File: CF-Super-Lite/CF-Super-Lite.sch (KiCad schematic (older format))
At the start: 12 parts, among them J1 IDE_CONNECTOR, J2 CF Adapter Power, J3 Bus_ISA_8bit, SW1 DIP Switch x3 or x4, U1 BIOS FLASH, U2 74HCT245, U3 GAL16V8

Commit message: CF-Super-Lite: Final board tweaks before sending to production.
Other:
- note removed: "TODO: Need to handle RESET signal."
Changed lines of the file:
@@
 NoConn ~ 2000 2000
 NoConn ~ 2000 2200
-Text Notes 750  6400 0    118  ~ 0
-TODO: Need to handle RESET signal.
 Text GLabel 4050 2300 0    50   Input ~ 0
 RESET

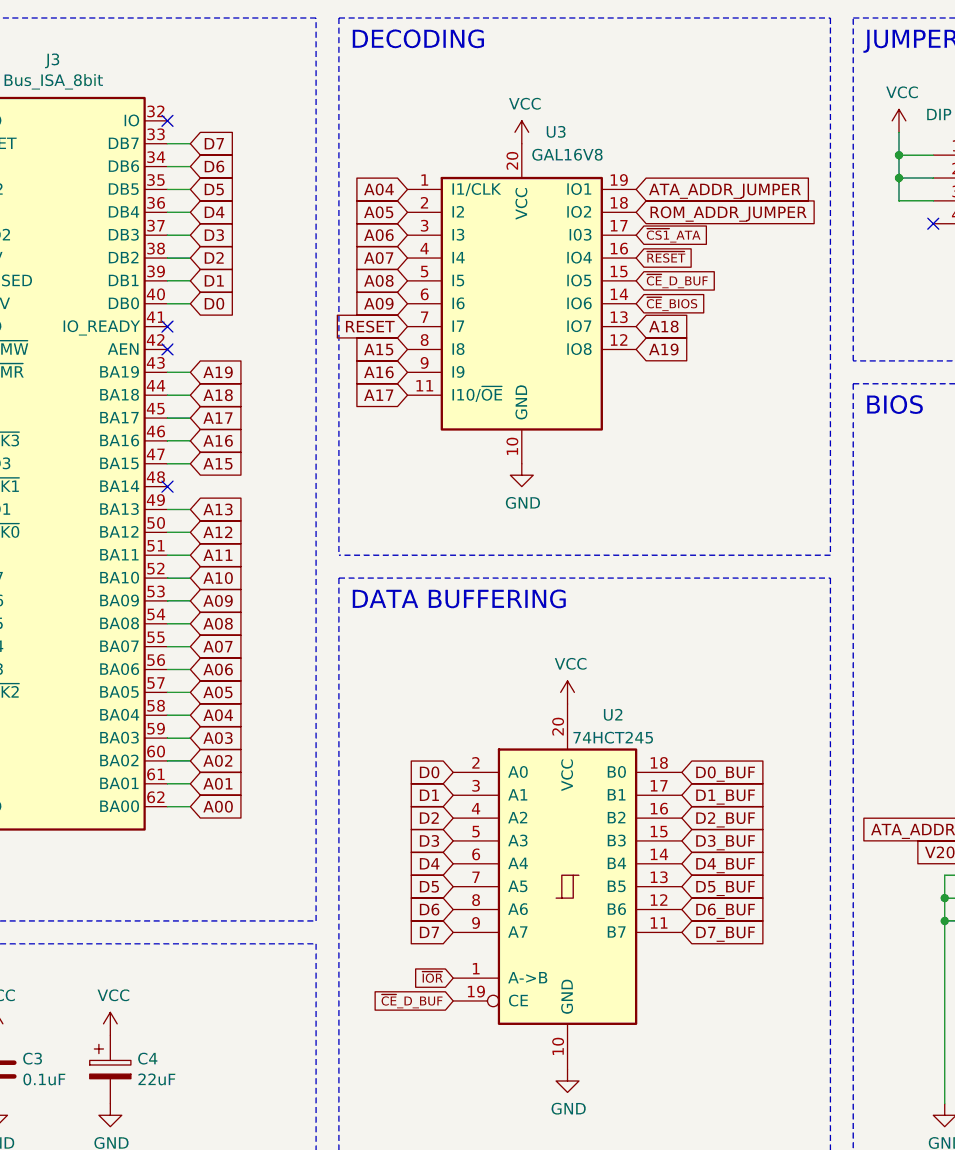
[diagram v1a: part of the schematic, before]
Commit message: CF-Super-Lite: Swap 16v8 GAL  for 22v10, add signals to generate correct buffer direction.
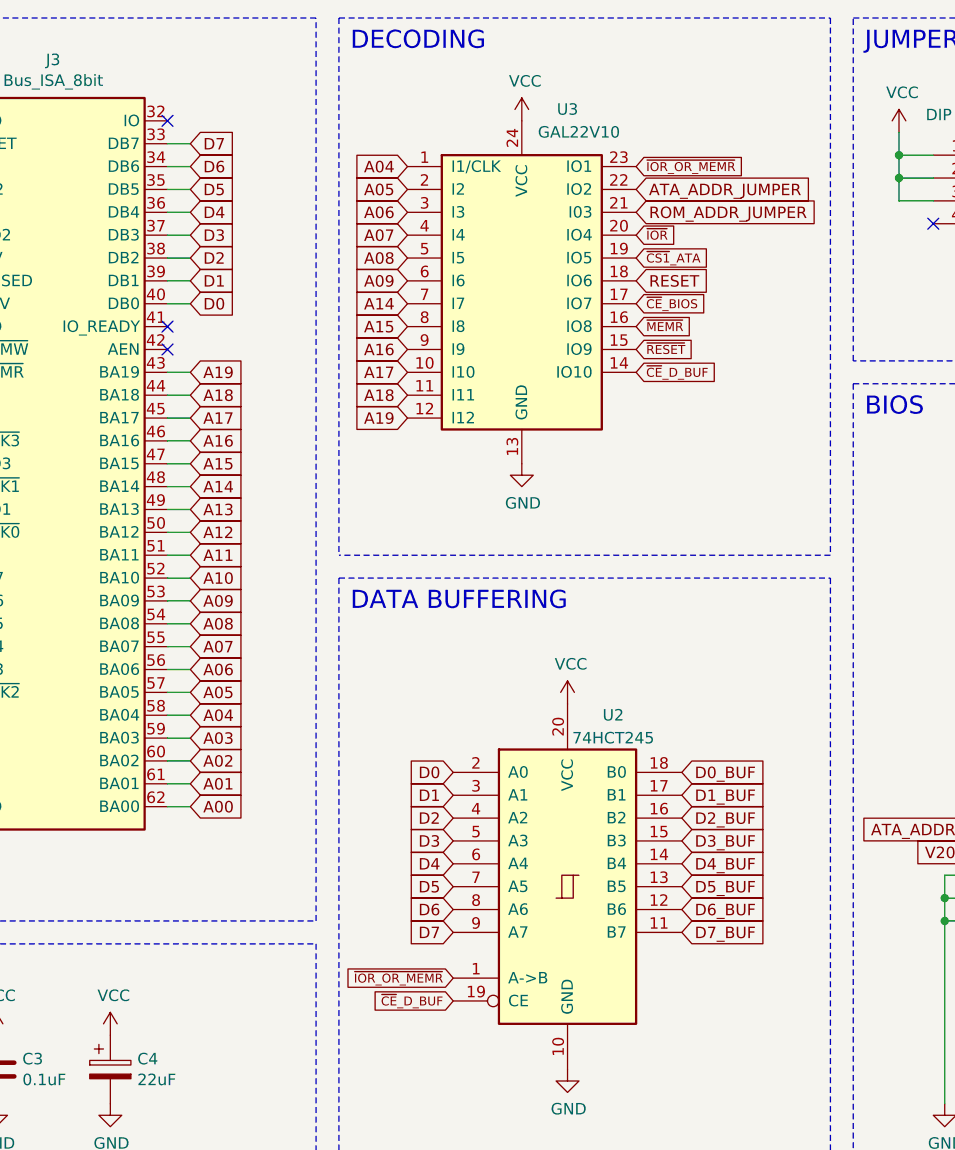
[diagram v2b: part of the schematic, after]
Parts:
- removed U3: GAL16V8, Package_DIP:DIP-20_W7.62mm_Socket, symbol Logic_Programmable:GAL16V8
- added U3: GAL22V10, Package_DIP:DIP-24_W7.62mm_Socket, symbol 00Common:GAL22V10
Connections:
- net A04: now also U3.1 (I1/CLK)
- net A05: now also U3.2 (I2)
- net A06: now also U3.3 (I3)
- net A07: now also U3.4 (I4)
- net A08: now also U3.5 (I5)
- net A09: now also U3.6 (I6)
- net A15: now also U3.8 (I8)
- net A16: now also U3.9 (I9)
- net A17: now also U3.10 (I10)
- net A18: now also U3.11 (I11)
- net A19: now also U3.12 (I12)
- net ATA_ADDR_JUMPER: now also U3.22 (IO2)
- net GND: now also U3.13 (GND)
- net RESET: now also U3.18 (IO6)
- net ROM_ADDR_JUMPER: now also U3.21 (I03)
- net VCC: now also U3.24 (VCC)
- net ~CE~_BIOS: now also U3.17 (IO7)
- net ~CE~_D_BUF: now also U3.14 (IO10)
- net ~CS1~_ATA: now also U3.19 (IO5)
- net ~IOR: now also U3.20 (IO4); no longer U2.1 (A->B)
- net ~MEMR: now also U3.16 (IO8)
- net ~RESET: now also U3.15 (IO9)
- net A14: now reaches J3.48 (BA14)
- net A14: now also U3.7 (I7)
- new net ~IOR_OR_MEMR: U2.1 (A->B), U3.23 (IO1)
- no-connect marks 43 -> 42
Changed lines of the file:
@@
-	1    0    0    -1
-$EndComp
-$Comp
-L 74xx:74LS245 U2
-U 1 1 603B775F
-P 4750 4750
-F 0 "U2" H 4950 5500 50  0000 C CNN
-F 1 "74HCT245" H 4950 5400 50  0000 C CNN
-F 2 "Package_DIP:DIP-20_W7.62mm_Socket" H 4750 4750 50  0001 C CNN
-F 3 "http://www.ti.com/lit/gpn/sn74LS245" H 4750 4750 50  0001 C CNN
-	1    4750 4750
-	1    0    0    -1
-$EndComp
-$Comp
-L Logic_Programmable:GAL16V8 U3
-U 1 1 603B89A9
-P 4550 2200
-F 0 "U3" H 4700 2950 50  0000 C CNN
-F 1 "GAL16V8" H 4750 2850 50  0000 C CNN
-F 2 "Package_DIP:DIP-20_W7.62mm_Socket" H 4550 2200 50  0001 C CNN
-F 3 "" H 4550 2200 50  0001 C CNN
-	1    4550 2200
 	1    0    0    -1
 $EndComp
@@
 Text GLabel 9250 1350 0    39   Input ~ 0
 ~RESET
-Text GLabel 4250 4250 0    50   Input ~ 0
-D0
-Text GLabel 4250 4350 0    50   Input ~ 0
-D1
-Text GLabel 4250 4450 0    50   Input ~ 0
-D2
-Text GLabel 4250 4550 0    50   Input ~ 0
-D3
-Text GLabel 4250 4650 0    50   Input ~ 0
-D4
-Text GLabel 4250 4750 0    50   Input ~ 0
-D5
-Text GLabel 4250 4850 0    50   Input ~ 0
-D6
-Text GLabel 4250 4950 0    50   Input ~ 0
-D7
-Text GLabel 5250 4250 2    50   Input ~ 0
-D0_BUF
-Text GLabel 5250 4350 2    50   Input ~ 0
-D1_BUF
-Text GLabel 5250 4450 2    50   Input ~ 0
-D2_BUF
-Text GLabel 5250 4550 2    50   Input ~ 0
-D3_BUF
-Text GLabel 5250 4650 2    50   Input ~ 0
-D4_BUF
-Text GLabel 5250 4750 2    50   Input ~ 0
-D5_BUF
-Text GLabel 5250 4850 2    50   Input ~ 0
-D6_BUF
-Text GLabel 5250 4950 2    50   Input ~ 0
-D7_BUF
-$Comp
-L power:VCC #PWR0108
-U 1 1 603F73EA
-P 4750 3950
-F 0 "#PWR0108" H 4750 3800 50  0001 C CNN
-F 1 "VCC" H 4765 4123 50  0000 C CNN
-F 2 "" H 4750 3950 50  0001 C CNN
-F 3 "" H 4750 3950 50  0001 C CNN
-	1    4750 3950
-	1    0    0    -1
-$EndComp
-$Comp
-L power:GND #PWR0109
-U 1 1 60418B5F
-P 4750 5550
-F 0 "#PWR0109" H 4750 5300 50  0001 C CNN
-F 1 "GND" H 4755 5377 50  0000 C CNN
-F 2 "" H 4750 5550 50  0001 C CNN
-F 3 "" H 4750 5550 50  0001 C CNN
-	1    4750 5550
-	1    0    0    -1
-$EndComp
 $Comp
 L power:GND #PWR0110
@@
 L power:VCC #PWR0111
 U 1 1 60419399
-P 4550 1500
-F 0 "#PWR0111" H 4550 1350 50  0001 C CNN
-F 1 "VCC" H 4565 1673 50  0000 C CNN
-F 2 "" H 4550 1500 50  0001 C CNN
-F 3 "" H 4550 1500 50  0001 C CNN
-	1    4550 1500
-	1    0    0    -1
-$EndComp
-Text GLabel 4250 5250 0    39   Input ~ 0
-~CE~_D_BUF
-Text GLabel 4250 5150 0    39   Input ~ 0
-~IOR
+P 4550 1400
+F 0 "#PWR0111" H 4550 1250 50  0001 C CNN
+F 1 "VCC" H 4565 1573 50  0000 C CNN
+F 2 "" H 4550 1400 50  0001 C CNN
+F 3 "" H 4550 1400 50  0001 C CNN
+	1    4550 1400
+	1    0    0    -1
+$EndComp
 Text GLabel 6800 3100 0    50   Input ~ 0
 A00
@@
 Text GLabel 8000 3800 2    50   Input ~ 0
 D7_BUF
-Text GLabel 5050 1900 2    39   Input ~ 0
+Text GLabel 5050 2000 2    39   Input ~ 0
 ~CS1~_ATA
-Text GLabel 5050 2000 2    39   Input ~ 0
+Text GLabel 5050 2400 2    39   Input ~ 0
 ~RESET
 Text GLabel 5050 2200 2    39   Input ~ 0
 ~CE~_BIOS
-Text GLabel 5050 2100 2    39   Input ~ 0
+Text GLabel 5050 2500 2    39   Input ~ 0
 ~CE~_D_BUF
 Text GLabel 3100 3800 2    50   Input ~ 0
@@
 Text GLabel 3100 4000 2    50   Input ~ 0
 A04
+Text GLabel 4050 1900 0    50   Input ~ 0
+A07
 Text GLabel 4050 2000 0    50   Input ~ 0
-A07
+A08
 Text GLabel 4050 2100 0    50   Input ~ 0
-A08
-Text GLabel 4050 2200 0    50   Input ~ 0
 A09
-Text GLabel 4050 1900 0    50   Input ~ 0
+Text GLabel 4050 1800 0    50   Input ~ 0
 A06
-Text GLabel 4050 1800 0    50   Input ~ 0
+Text GLabel 4050 1700 0    50   Input ~ 0
 A05
-Text GLabel 4050 1700 0    50   Input ~ 0
+Text GLabel 4050 1600 0    50   Input ~ 0
 A04
 Text GLabel 3100 2500 2    50   Input ~ 0
@@
 Text GLabel 3100 2900 2    50   Input ~ 0
 A15
-Text GLabel 5050 2400 2    50   Input ~ 0
+Text GLabel 4050 2700 0    50   Input ~ 0
 A19
-Text GLabel 5050 2300 2    50   Input ~ 0
+Text GLabel 4050 2600 0    50   Input ~ 0
 A18
-Text GLabel 4050 2600 0    50   Input ~ 0
+Text GLabel 4050 2500 0    50   Input ~ 0
 A17
-Text GLabel 4050 2500 0    50   Input ~ 0
+Text GLabel 4050 2400 0    50   Input ~ 0
 A16
-Text GLabel 4050 2400 0    50   Input ~ 0
+Text GLabel 4050 2300 0    50   Input ~ 0
 A15
-Text GLabel 5050 1800 2    50   Input ~ 0
-ROM_ADDR_JUMPER
-Text GLabel 5050 1700 2    50   Input ~ 0
-ATA_ADDR_JUMPER
 Text GLabel 6800 4600 0    50   Input ~ 0
 V20_JUMPER
@@
 NoConn ~ 2000 2000
 NoConn ~ 2000 2200
-Text GLabel 4050 2300 0    50   Input ~ 0
+Text GLabel 5050 2100 2    50   Input ~ 0
 RESET
 Wire Wire Line
@@
 Text GLabel 9250 3150 0    39   Input ~ 0
 ~CS1~_ATA
-NoConn ~ 3000 3000
+Text GLabel 4250 5250 0    39   Input ~ 0
+~CE~_D_BUF
+$Comp
+L power:GND #PWR0109
+U 1 1 60418B5F
+P 4750 5550
+F 0 "#PWR0109" H 4750 5300 50  0001 C CNN
+F 1 "GND" H 4755 5377 50  0000 C CNN
+F 2 "" H 4750 5550 50  0001 C CNN
+F 3 "" H 4750 5550 50  0001 C CNN
+	1    4750 5550
+	1    0    0    -1
+$EndComp
+$Comp
+L power:VCC #PWR0108
+U 1 1 603F73EA
+P 4750 3950
+F 0 "#PWR0108" H 4750 3800 50  0001 C CNN
+F 1 "VCC" H 4765 4123 50  0000 C CNN
+F 2 "" H 4750 3950 50  0001 C CNN
+F 3 "" H 4750 3950 50  0001 C CNN
+	1    4750 3950
+	1    0    0    -1
+$EndComp
+$Comp
+L 74xx:74LS245 U2
+U 1 1 603B775F
+P 4750 4750
+F 0 "U2" H 4950 5500 50  0000 C CNN
+F 1 "74HCT245" H 4950 5400 50  0000 C CNN
+F 2 "Package_DIP:DIP-20_W7.62mm_Socket" H 4750 4750 50  0001 C CNN
+F 3 "http://www.ti.com/lit/gpn/sn74LS245" H 4750 4750 50  0001 C CNN
+	1    4750 4750
+	1    0    0    -1
+$EndComp
+Text GLabel 5250 4950 2    50   Input ~ 0
+D7_BUF
+Text GLabel 5250 4850 2    50   Input ~ 0
+D6_BUF
+Text GLabel 5250 4750 2    50   Input ~ 0
+D5_BUF
+Text GLabel 5250 4650 2    50   Input ~ 0
+D4_BUF
+Text GLabel 5250 4550 2    50   Input ~ 0
+D3_BUF
+Text GLabel 5250 4450 2    50   Input ~ 0
+D2_BUF
+Text GLabel 5250 4350 2    50   Input ~ 0
+D1_BUF
+Text GLabel 5250 4250 2    50   Input ~ 0
+D0_BUF
+Text GLabel 4250 4950 0    50   Input ~ 0
+D7
+Text GLabel 4250 4850 0    50   Input ~ 0
+D6
+Text GLabel 4250 4750 0    50   Input ~ 0
+D5
+Text GLabel 4250 4650 0    50   Input ~ 0
+D4
+Text GLabel 4250 4550 0    50   Input ~ 0
+D3
+Text GLabel 4250 4450 0    50   Input ~ 0
+D2
+Text GLabel 4250 4350 0    50   Input ~ 0
+D1
+Text GLabel 4250 4250 0    50   Input ~ 0
+D0
+Text GLabel 4250 5150 0    39   Input ~ 0
+~IOR_OR_MEMR
+Text GLabel 5050 1800 2    50   Input ~ 0
+ROM_ADDR_JUMPER
+Text GLabel 5050 1700 2    50   Input ~ 0
+ATA_ADDR_JUMPER
+$Comp
+L 00Common:GAL22V10 U3
+U 1 1 604CA5F0
+P 4550 2100
+F 0 "U3" H 4750 2850 50  0000 C CNN
+F 1 "GAL22V10" H 4800 2750 50  0000 C CNN
+F 2 "Package_DIP:DIP-24_W7.62mm_Socket" H 4550 2100 50  0001 C CNN
+F 3 "" H 4550 2100 50  0001 C CNN
+	1    4550 2100
+	1    0    0    -1
+$EndComp
+Text GLabel 3100 3000 2    50   Input ~ 0
+A14
+Wire Wire Line
+	3000 3000 3100 3000
+Text GLabel 4050 2200 0    50   Input ~ 0
+A14
+Text GLabel 5050 1600 2    39   Input ~ 0
+~IOR_OR_MEMR
+Text GLabel 5050 1900 2    39   Input ~ 0
+~IOR
+Text GLabel 5050 2300 2    39   Input ~ 0
+~MEMR
 $EndSCHEMATC
